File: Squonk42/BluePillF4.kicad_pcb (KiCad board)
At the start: 2 copper layers, 53.3 x 22.9 mm, 198 parts, among them J1 MH20-1, J2 MH20-1, J3 MH_RA4-1, J4 47309-2651, J5 U02-BFD3111B0-009, Q1 IRLML6402, U1 AP2114HA-3.3TRG1, U2 AP2112K3.3-TRG1, U3 STM32F405RGT6, U4 SY6280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

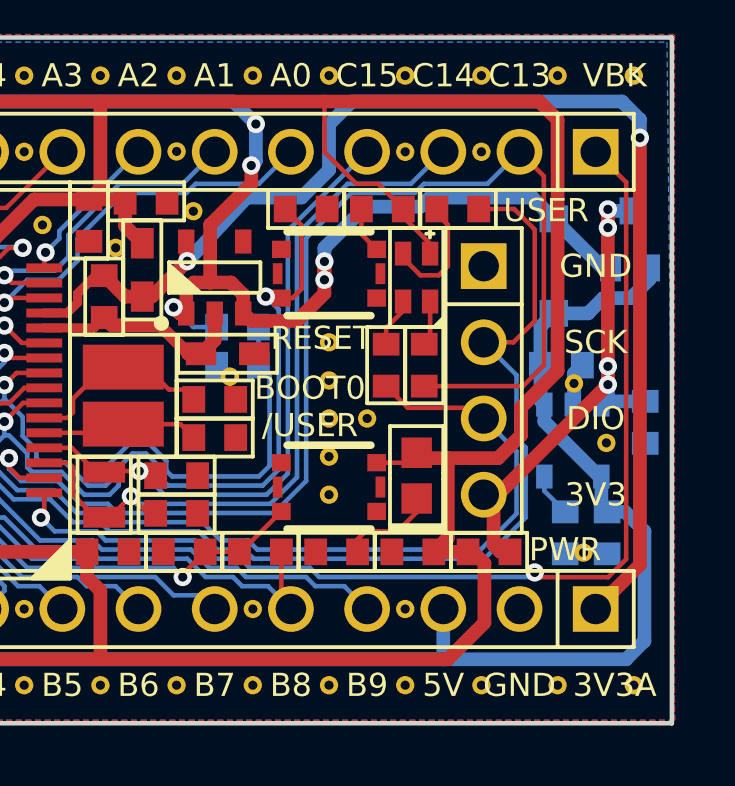
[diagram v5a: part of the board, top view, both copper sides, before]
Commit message: Applied suggested modifications by @victor_pv http://www.stm32duino.com/viewtopic.php?f=19&t=2633&p=40846#p40846
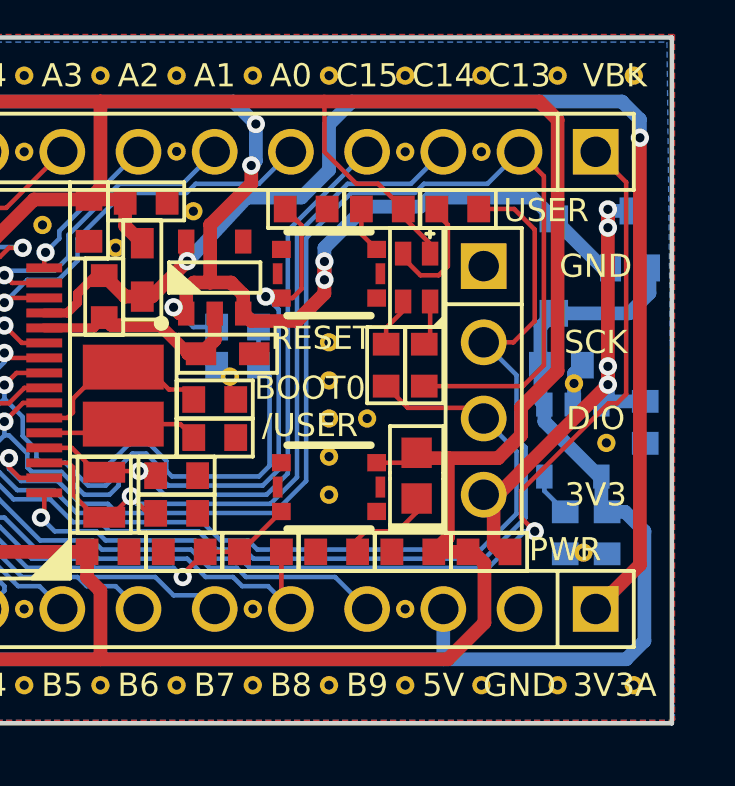
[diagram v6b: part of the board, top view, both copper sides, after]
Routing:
- net /BluePillF4-1/VBK: track 35.6 -> 33.4 mm
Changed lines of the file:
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@@
     (thickness 1.2)
     (drawings 115)
-    (tracks 1202)
+    (tracks 1199)
     (zones 0)
     (modules 198)
@@
   (title_block
     (title "BluePill F4")
-    (date 2018-02-02)
+    (date 2018-02-03)
     (rev A)
     (company www.stm32duino.com)
@@
   (layers
     (0 Top signal)
-    (31 Bottom signal)
+    (31 Bottom signal hide)
     (32 B.Adhes user hide)
     (33 F.Adhes user hide)
@@
   (segment (start 86.995 69.1515) (end 88.0635 69.1515) (width 0.4572) (layer Top) (net 2) (status 30))
   (segment (start 88.0635 69.1515) (end 88.508 69.596) (width 0.4572) (layer Top) (net 2) (status 30))
+  (segment (start 125.603 62.5348) (end 128.1176 62.5348) (width 0.4572) (layer Bottom) (net 3) (status 10))
+  (segment (start 128.793 61.8594) (end 128.793 61.021) (width 0.4572) (layer Bottom) (net 3) (status 20))
+  (segment (start 128.1176 62.5348) (end 128.793 61.8594) (width 0.4572) (layer Bottom) (net 3))
   (segment (start 82.9056 62.7888) (end 86.868 62.7888) (width 0.4572) (layer Bottom) (net 3))
   (segment (start 86.868 62.7888) (end 87.7824 61.8744) (width 0.4572) (layer Bottom) (net 3))
@@
   (segment (start 87.7824 61.8744) (end 88.392 61.8744) (width 0.4571) (layer Top) (net 3))
   (via (at 87.7824 61.8744) (size 0.6096) (drill 0.3048) (layers Top Bottom) (net 3))
-  (segment (start 128.793 61.021) (end 128.793 61.4014) (width 0.4572) (layer Bottom) (net 3) (status 30))
-  (segment (start 128.793 61.4014) (end 128.168 62.0264) (width 0.4572) (layer Bottom) (net 3) (status 10))
-  (segment (start 127.2536 62.0264) (end 128.168 62.0264) (width 0.4572) (layer Bottom) (net 3))
-  (segment (start 126.7452 62.5348) (end 125.603 62.5348) (width 0.4572) (layer Bottom) (net 3) (status 20))
-  (segment (start 127.2536 62.0264) (end 126.7452 62.5348) (width 0.4572) (layer Bottom) (net 3))
   (segment (start 125.1585 64.262) (end 125.1585 62.9793) (width 0.4572) (layer Bottom) (net 3) (status 30))
   (segment (start 125.1585 62.9793) (end 125.603 62.5348) (width 0.4572) (layer Bottom) (net 3) (status 30))
@@
   (segment (start 99.6696 60.198) (end 99.6696 60.3504) (width 0.1524) (layer Top) (net 36))
   (segment (start 100.12172 59.74588) (end 99.6696 60.198) (width 0.1524) (layer Top) (net 36))
-  (segment (start 106.8324 68.7324) (end 106.68 68.7324) (width 0.1524) (layer Top) (net 37))
-  (segment (start 105.61828 69.641792) (end 105.765672 69.4944) (width 0.1524) (layer Top) (net 37))
-  (segment (start 105.765672 69.4944) (end 105.918 69.4944) (width 0.1524) (layer Top) (net 37))
-  (segment (start 105.61828 70.51802) (end 105.61828 69.641792) (width 0.1524) (layer Top) (net 37) (status 10))
-  (segment (start 107.111056 68.7324) (end 108.482646 70.10399) (width 0.1524) (layer Bottom) (net 37))
-  (segment (start 108.482646 70.10399) (end 110.233014 70.10399) (width 0.1524) (layer Bottom) (net 37))
-  (segment (start 110.233014 70.10399) (end 110.537816 70.408792) (width 0.1524) (layer Bottom) (net 37))
-  (segment (start 110.537816 70.408792) (end 113.511848 70.408792) (width 0.1524) (layer Bottom) (net 37))
-  (segment (start 113.511848 70.408792) (end 114.121454 71.018398) (width 0.1524) (layer Bottom) (net 37))
-  (segment (start 114.121454 71.018398) (end 115.035854 71.018398) (width 0.1524) (layer Bottom) (net 37))
-  (segment (start 115.035854 71.018398) (end 115.340654 71.323198) (width 0.1524) (layer Bottom) (net 37))
-  (segment (start 115.340654 71.323198) (end 117.347998 71.323198) (width 0.1524) (layer Bottom) (net 37))
-  (segment (start 117.347998 71.323198) (end 117.6528 71.628) (width 0.1524) (layer Bottom) (net 37))
-  (segment (start 117.6528 71.628) (end 118.618 71.628) (width 0.1524) (layer Bottom) (net 37))
-  (segment (start 118.618 71.628) (end 119.38 72.39) (width 0.1524) (layer Bottom) (net 37) (status 20))
-  (via (at 106.8324 68.7324) (size 0.6096) (drill 0.3048) (layers Top Bottom) (net 37))
-  (segment (start 106.8324 68.7324) (end 107.111056 68.7324) (width 0.1524) (layer Bottom) (net 37))
+  (segment (start 115.340654 71.323198) (end 118.313198 71.323198) (width 0.1524) (layer Bottom) (net 37))
   (segment (start 106.68 68.7324) (end 105.918 69.4944) (width 0.1524) (layer Top) (net 37))
+  (segment (start 106.8324 68.7324) (end 107.111056 68.7324) (width 0.1524) (layer Bottom) (net 37))
+  (via (at 106.8324 68.7324) (size 0.6096) (drill 0.3048) (layers Top Bottom) (net 37))
+  (segment (start 115.035854 71.018398) (end 115.340654 71.323198) (width 0.1524) (layer Bottom) (net 37))
+  (segment (start 114.121454 71.018398) (end 115.035854 71.018398) (width 0.1524) (layer Bottom) (net 37))
+  (segment (start 113.511848 70.408792) (end 114.121454 71.018398) (width 0.1524) (layer Bottom) (net 37))
+  (segment (start 110.537816 70.408792) (end 113.511848 70.408792) (width 0.1524) (layer Bottom) (net 37))
+  (segment (start 110.233014 70.10399) (end 110.537816 70.408792) (width 0.1524) (layer Bottom) (net 37))
+  (segment (start 108.482646 70.10399) (end 110.233014 70.10399) (width 0.1524) (layer Bottom) (net 37))
+  (segment (start 107.111056 68.7324) (end 108.482646 70.10399) (width 0.1524) (layer Bottom) (net 37))
+  (segment (start 105.61828 70.51802) (end 105.61828 69.641792) (width 0.1524) (layer Top) (net 37) (status 10))
+  (segment (start 105.765672 69.4944) (end 105.918 69.4944) (width 0.1524) (layer Top) (net 37))
+  (segment (start 105.61828 69.641792) (end 105.765672 69.4944) (width 0.1524) (layer Top) (net 37))
+  (segment (start 106.8324 68.7324) (end 106.68 68.7324) (width 0.1524) (layer Top) (net 37))
+  (segment (start 118.313198 71.323198) (end 119.38 72.39) (width 0.1524) (layer Bottom) (net 37) (status 20))
   (segment (start 105.918 68.7324) (end 105.93968 68.7324) (width 0.1524) (layer Bottom) (net 38))
   (segment (start 105.1179 69.711116) (end 105.6132 69.215816) (width 0.1524) (layer Top) (net 38))
@@
   (segment (start 123.5964 70.2564) (end 123.5964 68.7578) (width 0.4572) (layer Top) (net 77) (status 20))
   (segment (start 123.5964 68.9102) (end 123.2662 68.58) (width 0.4572) (layer Top) (net 77) (status 30))
+  (segment (start 115.466908 71.018396) (end 123.41786 71.018396) (width 0.1524) (layer Bottom) (net 78))
   (segment (start 108.5088 69.342) (end 108.508812 69.342) (width 0.1524) (layer Bottom) (net 78))
-  (segment (start 125.127309 71.330109) (end 124.968 71.1708) (width 0.1524) (layer Top) (net 78))
   (segment (start 108.61802 69.23278) (end 108.5088 69.342) (width 0.1524) (layer Top) (net 78))
   (via (at 108.5088 69.342) (size 0.6096) (drill 0.3048) (layers Top Bottom) (net 78))
   (segment (start 108.61802 68.51904) (end 108.61802 69.23278) (width 0.1524) (layer Top) (net 78) (status 10))
   (segment (start 128.015898 58.165898) (end 127 57.15) (width 0.1524) (layer Top) (net 78) (status 20))
-  (segment (start 128.015898 70.72752) (end 128.015898 58.165898) (width 0.1524) (layer Top) (net 78))
-  (segment (start 127.413309 71.330109) (end 128.015898 70.72752) (width 0.1524) (layer Top) (net 78))
-  (segment (start 127.413309 71.330109) (end 125.127309 71.330109) (width 0.1524) (layer Top) (net 78))
-  (via (at 124.968 71.1708) (size 0.6096) (drill 0.3048) (layers Top Bottom) (net 78))
-  (segment (start 124.815602 71.323198) (end 124.968 71.1708) (width 0.1524) (layer Bottom) (net 78))
-  (segment (start 117.779054 71.323198) (end 124.815602 71.323198) (width 0.1524) (layer Bottom) (net 78))
-  (segment (start 117.474252 71.018396) (end 117.779054 71.323198) (width 0.1524) (layer Bottom) (net 78))
-  (segment (start 115.466908 71.018396) (end 117.474252 71.018396) (width 0.1524) (layer Bottom) (net 78))
   (segment (start 115.162108 70.713596) (end 115.466908 71.018396) (width 0.1524) (layer Bottom) (net 78))
   (segment (start 114.247708 70.713596) (end 115.162108 70.713596) (width 0.1524) (layer Bottom) (net 78))
@@
   (segment (start 108.966 69.799188) (end 110.359268 69.799188) (width 0.1524) (layer Bottom) (net 78))
   (segment (start 108.508812 69.342) (end 108.966 69.799188) (width 0.1524) (layer Bottom) (net 78))
+  (segment (start 128.015898 65.227302) (end 128.015898 58.165898) (width 0.1524) (layer Top) (net 78))
+  (segment (start 127.7112 65.532) (end 128.015898 65.227302) (width 0.1524) (layer Top) (net 78))
+  (segment (start 127.431682 65.532) (end 127.7112 65.532) (width 0.1524) (layer Top) (net 78))
+  (segment (start 124.5108 68.452882) (end 127.431682 65.532) (width 0.1524) (layer Top) (net 78))
+  (segment (start 124.5108 69.342) (end 124.5108 68.452882) (width 0.1524) (layer Top) (net 78))
+  (segment (start 124.968 69.7992) (end 124.5108 69.342) (width 0.1524) (layer Top) (net 78))
+  (via (at 124.968 69.7992) (size 0.6096) (drill 0.3048) (layers Top Bottom) (net 78))
+  (segment (start 124.637056 69.7992) (end 124.968 69.7992) (width 0.1524) (layer Bottom) (net 78))
+  (segment (start 123.41786 71.018396) (end 124.637056 69.7992) (width 0.1524) (layer Bottom) (net 78))
   (segment (start 104.2415 62.0152) (end 105.3222 62.0152) (width 0.1524) (layer Bottom) (net 79))
   (segment (start 103.11892 59.711064) (end 103.327202 59.919346) (width 0.1524) (layer Top) (net 79))
